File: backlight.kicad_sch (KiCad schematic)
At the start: 32 parts

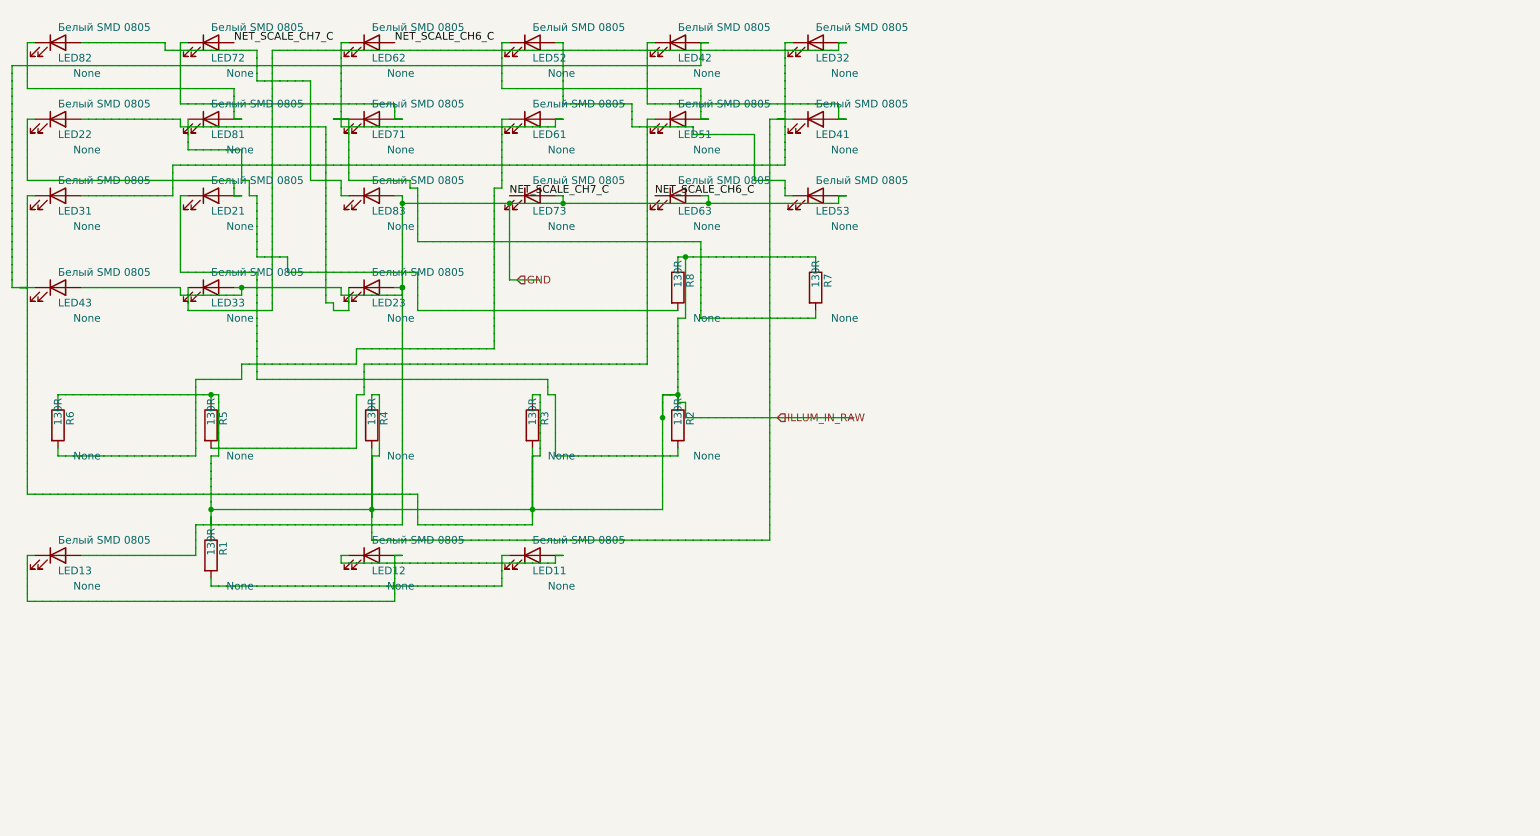
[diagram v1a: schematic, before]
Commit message: fix router map cell no more mark for pins
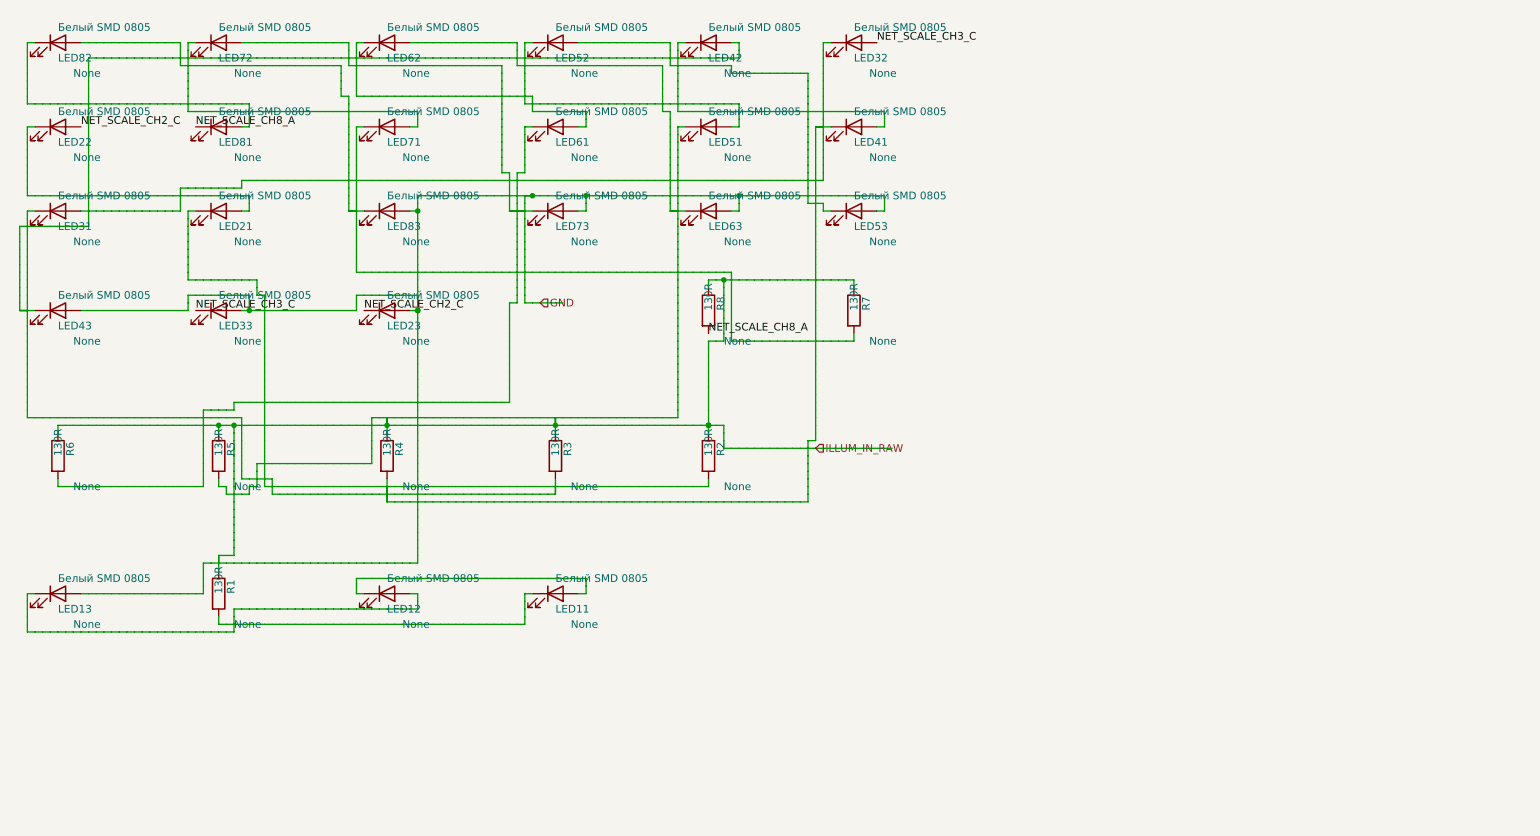
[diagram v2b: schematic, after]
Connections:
- net NET_SCALE_CH6_C is gone; now on net GND: LED62.2 (A), LED63.1 (K)
- net NET_SCALE_CH7_C is gone; now on net GND: LED72.2 (A), LED73.1 (K)
- net GND: no longer LED22.2 (A), LED23.1 (K), LED32.2 (A), LED33.1 (K), LED81.1 (K), R8.2
- net at LED11.1 (K), LED12.2 (A), LED13.1 (K)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: no longer LED11.2 (A), LED12.1 (K)
- new net: LED11.2 (A), LED12.1 (K)
- new net NET_SCALE_CH2_C: LED22.2 (A), LED23.1 (K)
- new net NET_SCALE_CH3_C: LED32.2 (A), LED33.1 (K)
- new net NET_SCALE_CH8_A: LED81.1 (K), R8.2

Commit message: рефакторинг проекта и начала прогона тестов
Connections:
- net GND: no longer LED52.2 (A), LED53.1 (K), LED62.2 (A), LED63.1 (K), LED72.2 (A), LED73.1 (K), LED82.2 (A), LED83.1 (K)
- new net NET_SCALE_CH5_C: LED52.2 (A), LED53.1 (K)
- new net NET_SCALE_CH6_C: LED62.2 (A), LED63.1 (K)
- new net NET_SCALE_CH7_C: LED72.2 (A), LED73.1 (K)
- new net NET_SCALE_CH8_C: LED82.2 (A), LED83.1 (K)

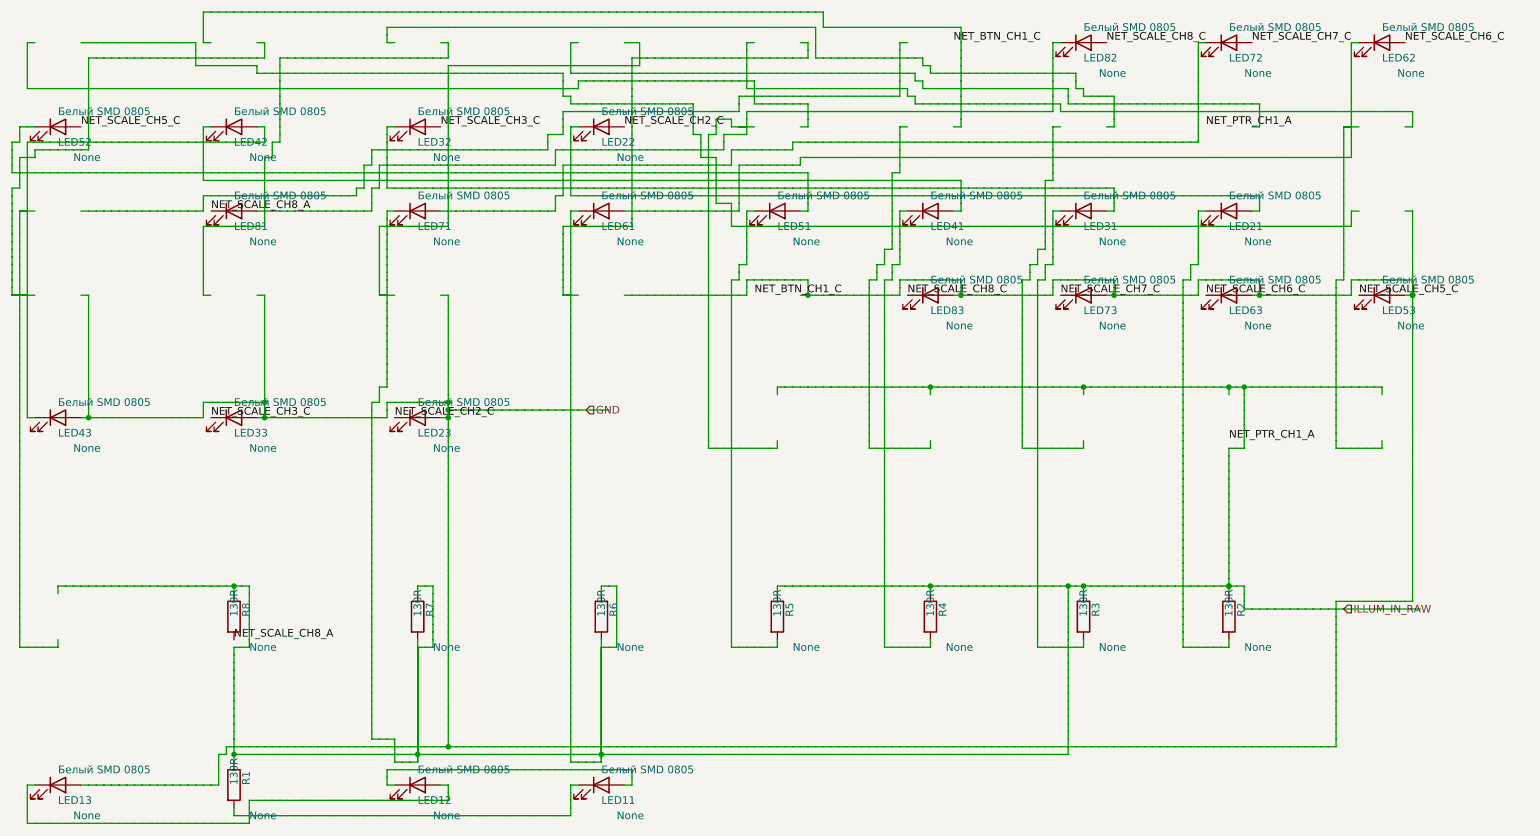
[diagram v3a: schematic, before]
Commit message: исправлены метки
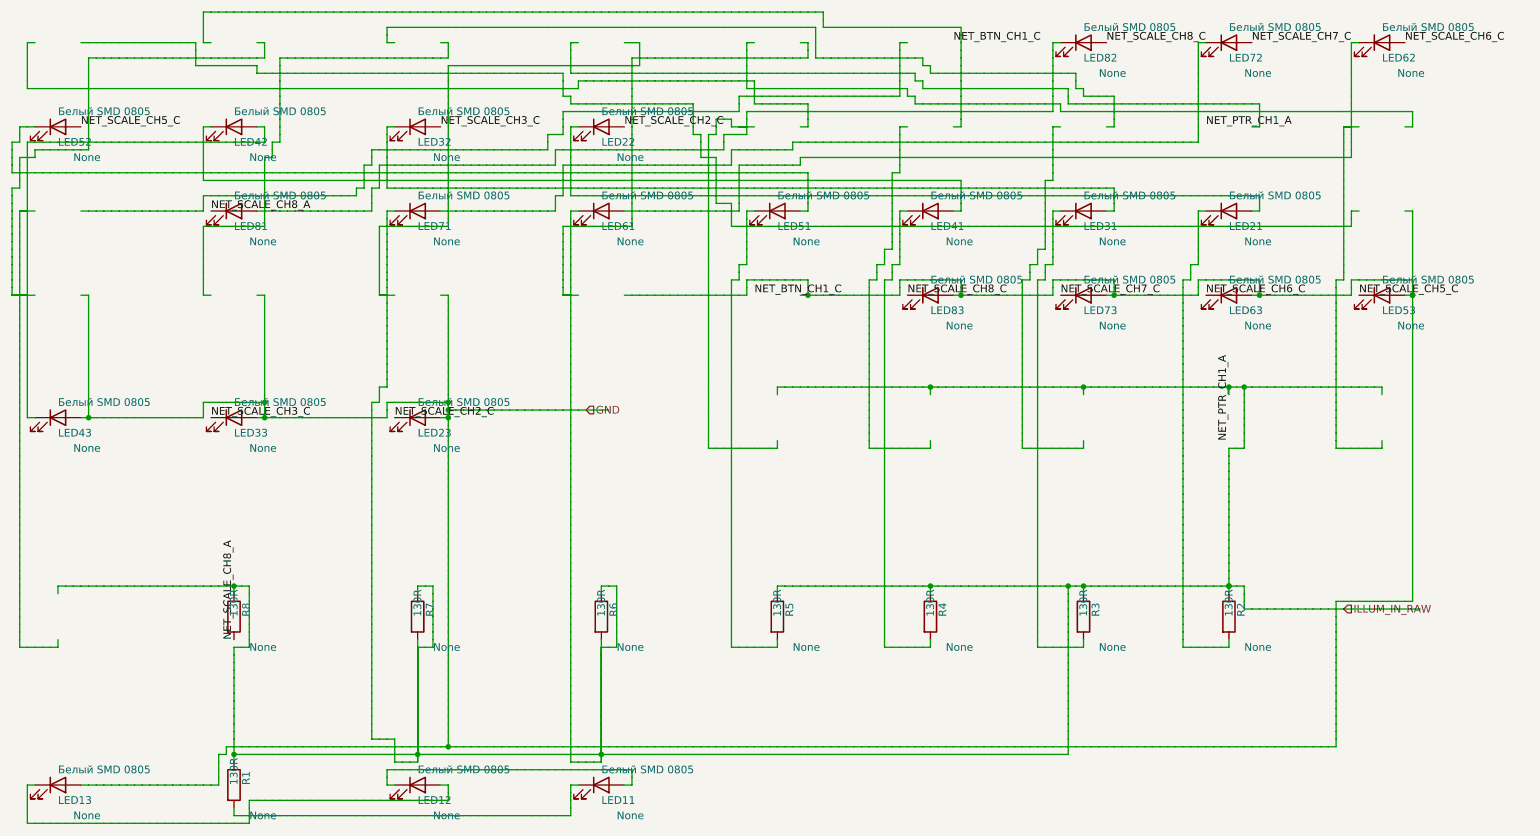
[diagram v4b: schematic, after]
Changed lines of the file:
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@@
 		(instances
 			(project "Untitled"
-				(path "/c51cc3a4-efd1-4e01-accf-2f7ce615c5b1"
+				(path "/a206513d-35e6-44c8-a0df-a219d1685167"
 					(reference "R1")
 					(unit 1)
@@
 		(instances
 			(project "Untitled"
-				(path "/c51cc3a4-efd1-4e01-accf-2f7ce615c5b1"
+				(path "/a206513d-35e6-44c8-a0df-a219d1685167"
 					(reference "R2")
 					(unit 1)
@@
 		(instances
 			(project "Untitled"
-				(path "/c51cc3a4-efd1-4e01-accf-2f7ce615c5b1"
+				(path "/a206513d-35e6-44c8-a0df-a219d1685167"
 					(reference "R3")
 					(unit 1)
@@
 		(instances
 			(project "Untitled"
-				(path "/c51cc3a4-efd1-4e01-accf-2f7ce615c5b1"
+				(path "/a206513d-35e6-44c8-a0df-a219d1685167"
 					(reference "R4")
 					(unit 1)
@@
 		(instances
 			(project "Untitled"
-				(path "/c51cc3a4-efd1-4e01-accf-2f7ce615c5b1"
+				(path "/a206513d-35e6-44c8-a0df-a219d1685167"
 					(reference "R5")
 					(unit 1)
@@
 		(instances
 			(project "Untitled"
-				(path "/c51cc3a4-efd1-4e01-accf-2f7ce615c5b1"
+				(path "/a206513d-35e6-44c8-a0df-a219d1685167"
 					(reference "R6")
 					(unit 1)
@@
 		(instances
 			(project "Untitled"
-				(path "/c51cc3a4-efd1-4e01-accf-2f7ce615c5b1"
+				(path "/a206513d-35e6-44c8-a0df-a219d1685167"
 					(reference "R7")
 					(unit 1)
@@
 		(instances
 			(project "Untitled"
-				(path "/c51cc3a4-efd1-4e01-accf-2f7ce615c5b1"
+				(path "/a206513d-35e6-44c8-a0df-a219d1685167"
 					(reference "R8")
 					(unit 1)
@@
 		(instances
 			(project "Untitled"
-				(path "/c51cc3a4-efd1-4e01-accf-2f7ce615c5b1"
+				(path "/a206513d-35e6-44c8-a0df-a219d1685167"
 					(reference "LED11")
 					(unit 1)
@@
 		(instances
 			(project "Untitled"
-				(path "/c51cc3a4-efd1-4e01-accf-2f7ce615c5b1"
+				(path "/a206513d-35e6-44c8-a0df-a219d1685167"
 					(reference "LED12")
 					(unit 1)
@@
 		(instances
 			(project "Untitled"
-				(path "/c51cc3a4-efd1-4e01-accf-2f7ce615c5b1"
+				(path "/a206513d-35e6-44c8-a0df-a219d1685167"
 					(reference "LED13")
 					(unit 1)
@@
 		(instances
 			(project "Untitled"
-				(path "/c51cc3a4-efd1-4e01-accf-2f7ce615c5b1"
+				(path "/a206513d-35e6-44c8-a0df-a219d1685167"
 					(reference "LED21")
 					(unit 1)
@@
 		(instances
 			(project "Untitled"
-				(path "/c51cc3a4-efd1-4e01-accf-2f7ce615c5b1"
+				(path "/a206513d-35e6-44c8-a0df-a219d1685167"
 					(reference "LED22")
 					(unit 1)
@@
 		(instances
 			(project "Untitled"
-				(path "/c51cc3a4-efd1-4e01-accf-2f7ce615c5b1"
+				(path "/a206513d-35e6-44c8-a0df-a219d1685167"
 					(reference "LED23")
 					(unit 1)
@@
 		(instances
 			(project "Untitled"
-				(path "/c51cc3a4-efd1-4e01-accf-2f7ce615c5b1"
+				(path "/a206513d-35e6-44c8-a0df-a219d1685167"
 					(reference "LED31")
 					(unit 1)
@@
 		(instances
 			(project "Untitled"
-				(path "/c51cc3a4-efd1-4e01-accf-2f7ce615c5b1"
+				(path "/a206513d-35e6-44c8-a0df-a219d1685167"
 					(reference "LED32")
 					(unit 1)
@@
 		(instances
 			(project "Untitled"
-				(path "/c51cc3a4-efd1-4e01-accf-2f7ce615c5b1"
+				(path "/a206513d-35e6-44c8-a0df-a219d1685167"
 					(reference "LED33")
 					(unit 1)
@@
 		(instances
 			(project "Untitled"
-				(path "/c51cc3a4-efd1-4e01-accf-2f7ce615c5b1"
+				(path "/a206513d-35e6-44c8-a0df-a219d1685167"
 					(reference "LED41")
 					(unit 1)
@@
 		(instances
 			(project "Untitled"
-				(path "/c51cc3a4-efd1-4e01-accf-2f7ce615c5b1"
+				(path "/a206513d-35e6-44c8-a0df-a219d1685167"
 					(reference "LED42")
 					(unit 1)
@@
 		(instances
 			(project "Untitled"
-				(path "/c51cc3a4-efd1-4e01-accf-2f7ce615c5b1"
+				(path "/a206513d-35e6-44c8-a0df-a219d1685167"
 					(reference "LED43")
 					(unit 1)
@@
 		(instances
 			(project "Untitled"
-				(path "/c51cc3a4-efd1-4e01-accf-2f7ce615c5b1"
+				(path "/a206513d-35e6-44c8-a0df-a219d1685167"
 					(reference "LED51")
 					(unit 1)
@@
 		(instances
 			(project "Untitled"
-				(path "/c51cc3a4-efd1-4e01-accf-2f7ce615c5b1"
+				(path "/a206513d-35e6-44c8-a0df-a219d1685167"
 					(reference "LED52")
 					(unit 1)
@@
 		(instances
 			(project "Untitled"
-				(path "/c51cc3a4-efd1-4e01-accf-2f7ce615c5b1"
+				(path "/a206513d-35e6-44c8-a0df-a219d1685167"
 					(reference "LED53")
 					(unit 1)
@@
 		(instances
 			(project "Untitled"
-				(path "/c51cc3a4-efd1-4e01-accf-2f7ce615c5b1"
+				(path "/a206513d-35e6-44c8-a0df-a219d1685167"
 					(reference "LED61")
 					(unit 1)
@@
 		(instances
 			(project "Untitled"
-				(path "/c51cc3a4-efd1-4e01-accf-2f7ce615c5b1"
+				(path "/a206513d-35e6-44c8-a0df-a219d1685167"
 					(reference "LED62")
 					(unit 1)
@@
 		(instances
 			(project "Untitled"
-				(path "/c51cc3a4-efd1-4e01-accf-2f7ce615c5b1"
+				(path "/a206513d-35e6-44c8-a0df-a219d1685167"
 					(reference "LED63")
 					(unit 1)
@@
 		(instances
 			(project "Untitled"
-				(path "/c51cc3a4-efd1-4e01-accf-2f7ce615c5b1"
+				(path "/a206513d-35e6-44c8-a0df-a219d1685167"
 					(reference "LED71")
 					(unit 1)
@@
 		(instances
 			(project "Untitled"
-				(path "/c51cc3a4-efd1-4e01-accf-2f7ce615c5b1"
+				(path "/a206513d-35e6-44c8-a0df-a219d1685167"
 					(reference "LED72")
 					(unit 1)
@@
 		(instances
 			(project "Untitled"
-				(path "/c51cc3a4-efd1-4e01-accf-2f7ce615c5b1"
+				(path "/a206513d-35e6-44c8-a0df-a219d1685167"
 					(reference "LED73")
 					(unit 1)
@@
 		(instances
 			(project "Untitled"
-				(path "/c51cc3a4-efd1-4e01-accf-2f7ce615c5b1"
+				(path "/a206513d-35e6-44c8-a0df-a219d1685167"
 					(reference "LED81")
 					(unit 1)
@@
 		(instances
 			(project "Untitled"
-				(path "/c51cc3a4-efd1-4e01-accf-2f7ce615c5b1"
+				(path "/a206513d-35e6-44c8-a0df-a219d1685167"
 					(reference "LED82")
 					(unit 1)
@@
 		(instances
 			(project "Untitled"
-				(path "/c51cc3a4-efd1-4e01-accf-2f7ce615c5b1"
+				(path "/a206513d-35e6-44c8-a0df-a219d1685167"
 					(reference "LED83")
 					(unit 1)
@@
 	)
 	(label "NET_SCALE_CH2_C"
-		(at 101.6 19.05 0)
+		(at 101.6 19.05 0.0000)
 		(effects
 			(font
@@
 	)
 	(label "NET_SCALE_CH2_C"
-		(at 63.5 67.31 0)
+		(at 63.5 67.31 180)
 		(effects
 			(font
@@
 	)
 	(label "NET_SCALE_CH3_C"
-		(at 71.12 19.05 0)
+		(at 71.12 19.05 0.0000)
 		(effects
 			(font
@@
 	)
 	(label "NET_SCALE_CH3_C"
-		(at 33.02 67.31 0)
+		(at 33.02 67.31 180)
 		(effects
 			(font
@@
 	)
 	(label "NET_SCALE_CH5_C"
-		(at 11.43 19.05 0)
+		(at 11.43 19.05 0.0000)
 		(effects
 			(font
@@
 	)
 	(label "NET_SCALE_CH5_C"
-		(at 223.52 46.99 0)
+		(at 223.52 46.99 180)
 		(effects
 			(font
@@
 	)
 	(label "NET_SCALE_CH6_C"
-		(at 231.14 5.08 0)
+		(at 231.14 5.08 0.0000)
 		(effects
 			(font
@@
 	)
 	(label "NET_SCALE_CH6_C"
-		(at 198.12 46.99 0)
+		(at 198.12 46.99 180)
 		(effects
 			(font
@@
 	)
 	(label "NET_SCALE_CH7_C"
-		(at 205.74 5.08 0)
+		(at 205.74 5.08 0.0000)
 		(effects
 			(font
@@
 	)
 	(label "NET_SCALE_CH7_C"
-		(at 173.99 46.99 0)
+		(at 173.99 46.99 180)
 		(effects
 			(font
@@
 	)
 	(label "NET_SCALE_CH8_A"
-		(at 36.83 104.14 0)
+		(at 36.83 104.14 270)
 		(effects
 			(font
@@
 	)
 	(label "NET_SCALE_CH8_A"
-		(at 33.02 33.02 0)
+		(at 33.02 33.02 180)
 		(effects
 			(font
@@
 	)
 	(label "NET_SCALE_CH8_C"
-		(at 181.61 5.08 0)
+		(at 181.61 5.08 0.0000)
 		(effects
 			(font
@@
 	)
 	(label "NET_SCALE_CH8_C"
-		(at 148.59 46.99 0)
+		(at 148.59 46.99 180)
 		(effects
 			(font
@@
 	)
 	(label "NET_BTN_CH1_C"
-		(at 156.21 5.08 0)
+		(at 156.21 5.08 0.0000)
 		(effects
 			(font
@@
 	)
 	(label "NET_BTN_CH1_C"
-		(at 123.19 46.99 0)
+		(at 123.19 46.99 180)
 		(effects
 			(font
@@
 	)
 	(label "NET_PTR_CH1_A"
-		(at 201.93 71.12 0)
+		(at 201.93 71.12 270)
 		(effects
 			(font
@@
 	)
 	(label "NET_PTR_CH1_A"
-		(at 198.12 19.05 0)
+		(at 198.12 19.05 180)
 		(effects
 			(font

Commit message: fix writer
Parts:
- added LED101, LED102, LED103, LED104, LED105, LED106: Белый SMD 1206, symbol Device:LED
- added LED201, LED202, LED203, LED204, LED205, LED206, LED207, LED208, LED209, LED210, LED211, LED212: Белый SMD 0603, symbol Device:LED
- added R10, R11, R12, R13, R14, R9: 130R, symbol Device:R
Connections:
- net GND: now also LED103.2 (A), LED106.2 (A), LED203.2 (A), LED206.2 (A), LED209.2 (A), LED212.2 (A); no longer LED21.1 (K), LED21.2 (A), LED22.1 (K), LED31.1 (K), LED31.2 (A), LED32.1 (K), LED41.1 (K), LED41.2 (A), LED42.1 (K), LED42.2 (A), LED43.1 (K), LED51.1 (K), LED51.2 (A), LED52.1 (K), LED61.1 (K), LED61.2 (A), LED62.1 (K), LED71.1 (K), LED71.2 (A), LED72.1 (K), LED81.2 (A), LED82.1 (K), R1.1, R2.1, R2.2, R3.1, R3.2, R4.1, R4.2, R5.1, R5.2, R6.1, R6.2, R7.1, R7.2, R8.1
- net NET_BTN_CH1_C: now also LED102.2 (A), LED103.1 (K)
- net NET_PTR_CH1_A: now also LED201.1 (K), R11.2
- net at LED11.1 (K), R1.2: no longer LED12.2 (A), LED13.1 (K)
- new net: LED101.1 (K), R9.2
- new net: LED204.1 (K), R12.2
- new net: LED204.2 (A), LED205.1 (K)
- new net: LED207.1 (K), R13.2
- new net: LED207.2 (A), LED208.1 (K)
- new net: LED205.2 (A), LED206.1 (K)
- new net: LED21.1 (K), R2.2
- new net: LED21.2 (A), LED22.1 (K)
- new net: LED81.2 (A), LED82.1 (K)
- new net: LED51.1 (K), R5.2
- new net: LED208.2 (A), LED209.1 (K)
- new net: LED202.2 (A), LED203.1 (K)
- new net: LED101.2 (A), LED102.1 (K)
- new net: LED41.2 (A), LED42.1 (K)
- new net: LED42.2 (A), LED43.1 (K)
- new net: LED201.2 (A), LED202.1 (K)
- new net: LED104.1 (K), R10.2
- new net: LED104.2 (A), LED105.1 (K)
- new net: LED41.1 (K), R4.2
- new net: LED105.2 (A), LED106.1 (K)
- new net: LED71.2 (A), LED72.1 (K)
- new net: LED31.1 (K), R3.2
- new net: LED31.2 (A), LED32.1 (K)
- new net: LED210.1 (K), R14.2
- new net: LED61.2 (A), LED62.1 (K)
- new net: LED51.2 (A), LED52.1 (K)
- new net: LED210.2 (A), LED211.1 (K)
- new net: LED211.2 (A), LED212.1 (K)
- new net: LED12.2 (A), LED13.1 (K)
- new net ILLUM_IN_RAW: LED61.1 (K), LED71.1 (K), R1.1, R10.1, R11.1, R12.1, R13.1, R14.1, R2.1, R3.1, R4.1, R5.1, R6.1, R6.2, R7.1, R7.2, R8.1, R9.1
